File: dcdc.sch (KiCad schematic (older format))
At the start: 0 parts

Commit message: Added charge pump IC REG71050
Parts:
- added C1, C2: 2.2uF, symbol Device:C_Small
- added C3: 220nF, symbol Device:C_Small
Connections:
- new net +3V3: C1.1
- new net +5V: C2.1
- new net GNDREF: C1.2, C2.2
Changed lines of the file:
@@
 $Descr A4 11693 8268
 encoding utf-8
-Sheet 4 8
+Sheet 4 11
 Title ""
 Date ""
@@
 Comment4 ""
 $EndDescr
+$Comp
+L Matthias:REG71050 #U05
+U 1 1 5BCCE2ED
+P 5800 3700
+F 0 "#U05" H 5500 3300 50  0000 C CNN
+F 1 "REG71050" H 5650 4000 50  0000 C CNN
+F 2 "" H 5600 3700 50  0001 C CNN
+F 3 "" H 5600 3700 50  0001 C CNN
+	1    5800 3700
+	1    0    0    -1
+$EndComp
+$Comp
+L power:+3V3 #PWR0109
+U 1 1 5BCCE361
+P 4600 3500
+F 0 "#PWR0109" H 4600 3350 50  0001 C CNN
+F 1 "+3V3" H 4615 3673 50  0000 C CNN
+F 2 "" H 4600 3500 50  0001 C CNN
+F 3 "" H 4600 3500 50  0001 C CNN
+	1    4600 3500
+	1    0    0    -1
+$EndComp
+$Comp
+L power:+5V #PWR0110
+U 1 1 5BCCE38F
+P 7250 3450
+F 0 "#PWR0110" H 7250 3300 50  0001 C CNN
+F 1 "+5V" H 7265 3623 50  0000 C CNN
+F 2 "" H 7250 3450 50  0001 C CNN
+F 3 "" H 7250 3450 50  0001 C CNN
+	1    7250 3450
+	1    0    0    -1
+$EndComp
+$Comp
+L Device:C_Small C3
+U 1 1 5BCCE42B
+P 6600 3900
+F 0 "C3" H 6692 3946 50  0000 L CNN
+F 1 "220nF" H 6692 3855 50  0000 L CNN
+F 2 "" H 6600 3900 50  0001 C CNN
+F 3 "~" H 6600 3900 50  0001 C CNN
+	1    6600 3900
+	1    0    0    -1
+$EndComp
+Wire Wire Line
+	5350 3700 5250 3700
+Wire Wire Line
+	4600 3700 4600 3500
+Wire Wire Line
+	5350 3550 5250 3550
+Wire Wire Line
+	5250 3550 5250 3700
+Connection ~ 5250 3700
+Wire Wire Line
+	5250 3700 4600 3700
+Wire Wire Line
+	5350 3950 5250 3950
+Wire Wire Line
+	5250 3950 5250 4100
+$Comp
+L power:GNDREF #PWR0111
+U 1 1 5BCCE4F1
+P 5250 4100
+F 0 "#PWR0111" H 5250 3850 50  0001 C CNN
+F 1 "GNDREF" H 5255 3927 50  0000 C CNN
+F 2 "" H 5250 4100 50  0001 C CNN
+F 3 "" H 5250 4100 50  0001 C CNN
+	1    5250 4100
+	1    0    0    -1
+$EndComp
+Wire Wire Line
+	6250 3850 6400 3850
+Wire Wire Line
+	6400 3850 6400 3800
+Wire Wire Line
+	6400 3800 6600 3800
+Wire Wire Line
+	6250 3950 6400 3950
+Wire Wire Line
+	6400 3950 6400 4000
+Wire Wire Line
+	6400 4000 6600 4000
+$Comp
+L Device:C_Small C1
+U 1 1 5BCCE887
+P 4600 3800
+F 0 "C1" H 4692 3846 50  0000 L CNN
+F 1 "2.2uF" H 4692 3755 50  0000 L CNN
+F 2 "" H 4600 3800 50  0001 C CNN
+F 3 "~" H 4600 3800 50  0001 C CNN
+	1    4600 3800
+	1    0    0    -1
+$EndComp
+Connection ~ 4600 3700
+$Comp
+L Device:C_Small C2
+U 1 1 5BCCE8E1
+P 7250 3800
+F 0 "C2" H 7342 3846 50  0000 L CNN
+F 1 "2.2uF" H 7342 3755 50  0000 L CNN
+F 2 "" H 7250 3800 50  0001 C CNN
+F 3 "~" H 7250 3800 50  0001 C CNN
+	1    7250 3800
+	1    0    0    -1
+$EndComp
+Wire Wire Line
+	6250 3700 7250 3700
+Wire Wire Line
+	7250 3700 7250 3450
+Connection ~ 7250 3700
+$Comp
+L power:GNDREF #PWR0112
+U 1 1 5BCCEAA5
+P 4600 3900
+F 0 "#PWR0112" H 4600 3650 50  0001 C CNN
+F 1 "GNDREF" H 4605 3727 50  0000 C CNN
+F 2 "" H 4600 3900 50  0001 C CNN
+F 3 "" H 4600 3900 50  0001 C CNN
+	1    4600 3900
+	1    0    0    -1
+$EndComp
+$Comp
+L power:GNDREF #PWR0113
+U 1 1 5BCCEAB8
+P 7250 3900
+F 0 "#PWR0113" H 7250 3650 50  0001 C CNN
+F 1 "GNDREF" H 7255 3727 50  0000 C CNN
+F 2 "" H 7250 3900 50  0001 C CNN
+F 3 "" H 7250 3900 50  0001 C CNN
+	1    7250 3900
+	1    0    0    -1
+$EndComp
 $EndSCHEMATC

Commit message: Assigned footprints
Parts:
- C1, C2, C3: footprint (none) -> Capacitor_SMD:C_0805_2012Metric_Pad1.15x1.40mm_HandSolder
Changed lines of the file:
@@
 F 0 "#U05" H 5500 3300 50  0000 C CNN
 F 1 "REG71050" H 5650 4000 50  0000 C CNN
-F 2 "" H 5600 3700 50  0001 C CNN
+F 2 "Package_TO_SOT_SMD:SOT-23-6_Handsoldering" H 5600 3700 50  0001 C CNN
 F 3 "" H 5600 3700 50  0001 C CNN
 	1    5800 3700
@@
 F 0 "C3" H 6692 3946 50  0000 L CNN
 F 1 "220nF" H 6692 3855 50  0000 L CNN
-F 2 "" H 6600 3900 50  0001 C CNN
+F 2 "Capacitor_SMD:C_0805_2012Metric_Pad1.15x1.40mm_HandSolder" H 6600 3900 50  0001 C CNN
 F 3 "~" H 6600 3900 50  0001 C CNN
 	1    6600 3900
@@
 F 0 "C1" H 4692 3846 50  0000 L CNN
 F 1 "2.2uF" H 4692 3755 50  0000 L CNN
-F 2 "" H 4600 3800 50  0001 C CNN
+F 2 "Capacitor_SMD:C_0805_2012Metric_Pad1.15x1.40mm_HandSolder" H 4600 3800 50  0001 C CNN
 F 3 "~" H 4600 3800 50  0001 C CNN
 	1    4600 3800
@@
 F 0 "C2" H 7342 3846 50  0000 L CNN
 F 1 "2.2uF" H 7342 3755 50  0000 L CNN
-F 2 "" H 7250 3800 50  0001 C CNN
+F 2 "Capacitor_SMD:C_0805_2012Metric_Pad1.15x1.40mm_HandSolder" H 7250 3800 50  0001 C CNN
 F 3 "~" H 7250 3800 50  0001 C CNN
 	1    7250 3800

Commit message: Began layouting
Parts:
- added U5: REG71050, Package_TO_SOT_SMD:SOT-23-6_Handsoldering, symbol Matthias:REG71050
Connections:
- net +3V3: now also U5.3 (EN), U5.5 (V_IN)
- net +5V: now also U5.1 (V_OUT)
- net GNDREF: now also U5.2 (GND)
- net at C3.1: now also U5.4 (C_PUMP_A)
- net at C3.2: now also U5.6 (C_PUMP_B)
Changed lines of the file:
@@
 $EndDescr
 $Comp
-L Matthias:REG71050 #U05
+L Matthias:REG71050 U5
 U 1 1 5BCCE2ED
 P 5800 3700
-F 0 "#U05" H 5500 3300 50  0000 C CNN
+F 0 "U5" H 5500 3300 50  0000 C CNN
 F 1 "REG71050" H 5650 4000 50  0000 C CNN
 F 2 "Package_TO_SOT_SMD:SOT-23-6_Handsoldering" H 5600 3700 50  0001 C CNN

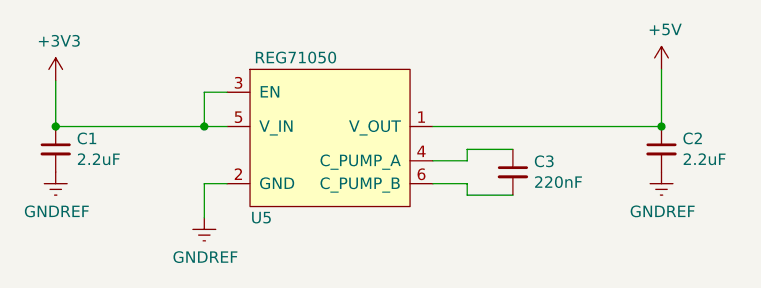
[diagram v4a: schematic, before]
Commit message: Continued layouting
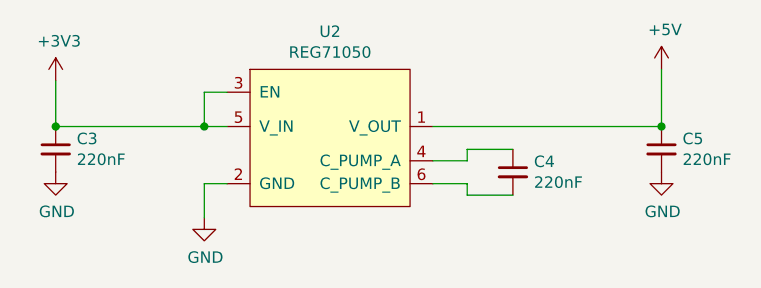
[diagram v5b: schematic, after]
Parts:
- removed C1, C2: 2.2uF, Capacitor_SMD:C_0805_2012Metric_Pad1.15x1.40mm_HandSolder, symbol Device:C_Small
- removed U5: REG71050, Package_TO_SOT_SMD:SOT-23-6_Handsoldering, symbol Matthias:REG71050
- added C3, C5: 220nF, Capacitor_SMD:C_0805_2012Metric_Pad1.15x1.40mm_HandSolder, symbol Device:C_Small
- added U2: REG71050, Package_TO_SOT_SMD:SOT-23-6_Handsoldering, symbol Matthias:REG71050
- renumbered C3 to C4
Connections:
- net +3V3: now also C3.1, U2.3 (EN), U2.5 (V_IN)
- net +5V: now also C5.1, U2.1 (V_OUT)
- net at C4.1: now also U2.4 (C_PUMP_A)
- net at C4.2: now also U2.6 (C_PUMP_B)
- new net GND: C3.2, C5.2, U2.2 (GND)
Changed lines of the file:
@@
 $EndDescr
 $Comp
-L Matthias:REG71050 U5
-U 1 1 5BCCE2ED
-P 5800 3700
-F 0 "U5" H 5500 3300 50  0000 C CNN
-F 1 "REG71050" H 5650 4000 50  0000 C CNN
-F 2 "Package_TO_SOT_SMD:SOT-23-6_Handsoldering" H 5600 3700 50  0001 C CNN
-F 3 "" H 5600 3700 50  0001 C CNN
-	1    5800 3700
-	1    0    0    -1
-$EndComp
-$Comp
-L power:+3V3 #PWR0109
+L power:+3V3 #PWR013
 U 1 1 5BCCE361
 P 4600 3500
-F 0 "#PWR0109" H 4600 3350 50  0001 C CNN
+F 0 "#PWR013" H 4600 3350 50  0001 C CNN
 F 1 "+3V3" H 4615 3673 50  0000 C CNN
 F 2 "" H 4600 3500 50  0001 C CNN
@@
 $EndComp
 $Comp
-L power:+5V #PWR0110
+L power:+5V #PWR016
 U 1 1 5BCCE38F
 P 7250 3450
-F 0 "#PWR0110" H 7250 3300 50  0001 C CNN
+F 0 "#PWR016" H 7250 3300 50  0001 C CNN
 F 1 "+5V" H 7265 3623 50  0000 C CNN
 F 2 "" H 7250 3450 50  0001 C CNN
@@
 $EndComp
 $Comp
-L Device:C_Small C3
+L Device:C_Small C4
 U 1 1 5BCCE42B
 P 6600 3900
-F 0 "C3" H 6692 3946 50  0000 L CNN
+F 0 "C4" H 6692 3946 50  0000 L CNN
 F 1 "220nF" H 6692 3855 50  0000 L CNN
 F 2 "Capacitor_SMD:C_0805_2012Metric_Pad1.15x1.40mm_HandSolder" H 6600 3900 50  0001 C CNN
@@
 Wire Wire Line
 	5250 3950 5250 4100
-$Comp
-L power:GNDREF #PWR0111
-U 1 1 5BCCE4F1
-P 5250 4100
-F 0 "#PWR0111" H 5250 3850 50  0001 C CNN
-F 1 "GNDREF" H 5255 3927 50  0000 C CNN
-F 2 "" H 5250 4100 50  0001 C CNN
-F 3 "" H 5250 4100 50  0001 C CNN
-	1    5250 4100
-	1    0    0    -1
-$EndComp
 Wire Wire Line
 	6250 3850 6400 3850
@@
 Wire Wire Line
 	6400 4000 6600 4000
+Wire Wire Line
+	6250 3700 7250 3700
+Wire Wire Line
+	7250 3700 7250 3450
 $Comp
-L Device:C_Small C1
-U 1 1 5BCCE887
+L Matthias:REG71050 U2
+U 1 1 5BCF6E97
+P 5800 3700
+F 0 "U2" H 5800 4115 50  0000 C CNN
+F 1 "REG71050" H 5800 4024 50  0000 C CNN
+F 2 "Package_TO_SOT_SMD:SOT-23-6_Handsoldering" H 5600 3700 50  0001 C CNN
+F 3 "" H 5600 3700 50  0001 C CNN
+	1    5800 3700
+	1    0    0    -1
+$EndComp
+$Comp
+L power:GND #PWR017
+U 1 1 5BCF70B8
+P 7250 3900
+F 0 "#PWR017" H 7250 3650 50  0001 C CNN
+F 1 "GND" H 7255 3727 50  0000 C CNN
+F 2 "" H 7250 3900 50  0001 C CNN
+F 3 "" H 7250 3900 50  0001 C CNN
+	1    7250 3900
+	1    0    0    -1
+$EndComp
+$Comp
+L power:GND #PWR015
+U 1 1 5BCF70D2
+P 5250 4100
+F 0 "#PWR015" H 5250 3850 50  0001 C CNN
+F 1 "GND" H 5255 3927 50  0000 C CNN
+F 2 "" H 5250 4100 50  0001 C CNN
+F 3 "" H 5250 4100 50  0001 C CNN
+	1    5250 4100
+	1    0    0    -1
+$EndComp
+$Comp
+L power:GND #PWR014
+U 1 1 5BCF70E5
+P 4600 3900
+F 0 "#PWR014" H 4600 3650 50  0001 C CNN
+F 1 "GND" H 4605 3727 50  0000 C CNN
+F 2 "" H 4600 3900 50  0001 C CNN
+F 3 "" H 4600 3900 50  0001 C CNN
+	1    4600 3900
+	1    0    0    -1
+$EndComp
+$Comp
+L Device:C_Small C5
+U 1 1 5BCF742B
+P 7250 3800
+F 0 "C5" H 7342 3846 50  0000 L CNN
+F 1 "220nF" H 7342 3755 50  0000 L CNN
+F 2 "Capacitor_SMD:C_0805_2012Metric_Pad1.15x1.40mm_HandSolder" H 7250 3800 50  0001 C CNN
+F 3 "~" H 7250 3800 50  0001 C CNN
+	1    7250 3800
+	1    0    0    -1
+$EndComp
+Connection ~ 7250 3700
+$Comp
+L Device:C_Small C3
+U 1 1 5BCF7461
 P 4600 3800
-F 0 "C1" H 4692 3846 50  0000 L CNN
-F 1 "2.2uF" H 4692 3755 50  0000 L CNN
+F 0 "C3" H 4692 3846 50  0000 L CNN
+F 1 "220nF" H 4692 3755 50  0000 L CNN
 F 2 "Capacitor_SMD:C_0805_2012Metric_Pad1.15x1.40mm_HandSolder" H 4600 3800 50  0001 C CNN
 F 3 "~" H 4600 3800 50  0001 C CNN
@@
 $EndComp
 Connection ~ 4600 3700
-$Comp
-L Device:C_Small C2
-U 1 1 5BCCE8E1
-P 7250 3800
-F 0 "C2" H 7342 3846 50  0000 L CNN
-F 1 "2.2uF" H 7342 3755 50  0000 L CNN
-F 2 "Capacitor_SMD:C_0805_2012Metric_Pad1.15x1.40mm_HandSolder" H 7250 3800 50  0001 C CNN
-F 3 "~" H 7250 3800 50  0001 C CNN
-	1    7250 3800
-	1    0    0    -1
-$EndComp
-Wire Wire Line
-	6250 3700 7250 3700
-Wire Wire Line
-	7250 3700 7250 3450
-Connection ~ 7250 3700
-$Comp
-L power:GNDREF #PWR0112
-U 1 1 5BCCEAA5
-P 4600 3900
-F 0 "#PWR0112" H 4600 3650 50  0001 C CNN
-F 1 "GNDREF" H 4605 3727 50  0000 C CNN
-F 2 "" H 4600 3900 50  0001 C CNN
-F 3 "" H 4600 3900 50  0001 C CNN
-	1    4600 3900
-	1    0    0    -1
-$EndComp
-$Comp
-L power:GNDREF #PWR0113
-U 1 1 5BCCEAB8
-P 7250 3900
-F 0 "#PWR0113" H 7250 3650 50  0001 C CNN
-F 1 "GNDREF" H 7255 3727 50  0000 C CNN
-F 2 "" H 7250 3900 50  0001 C CNN
-F 3 "" H 7250 3900 50  0001 C CNN
-	1    7250 3900
-	1    0    0    -1
-$EndComp
 $EndSCHEMATC

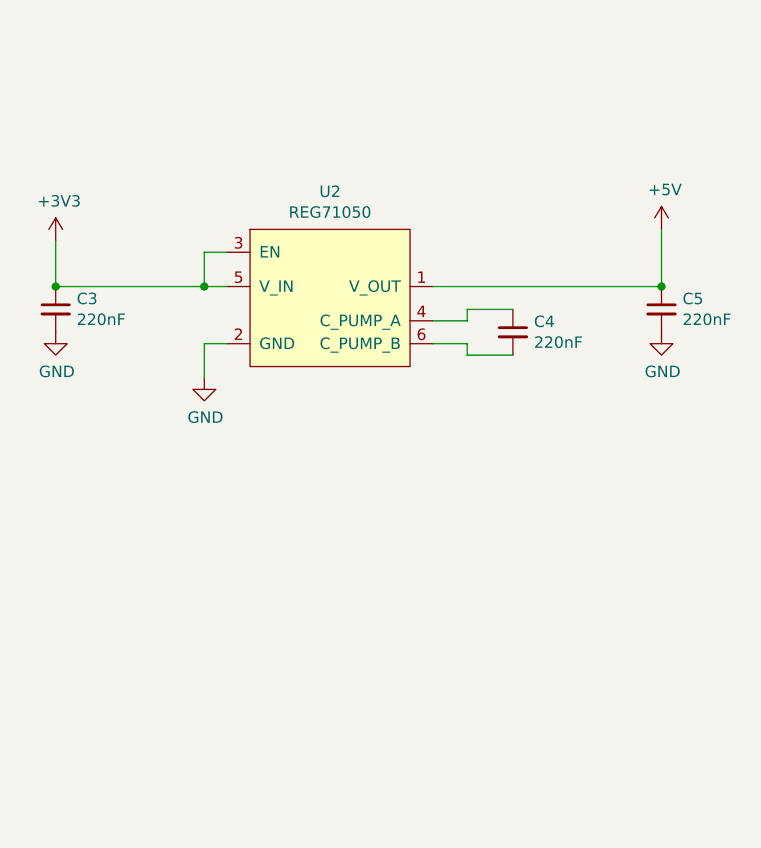
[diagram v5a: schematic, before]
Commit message: Updated RJ45 symbol and corresponding signal names
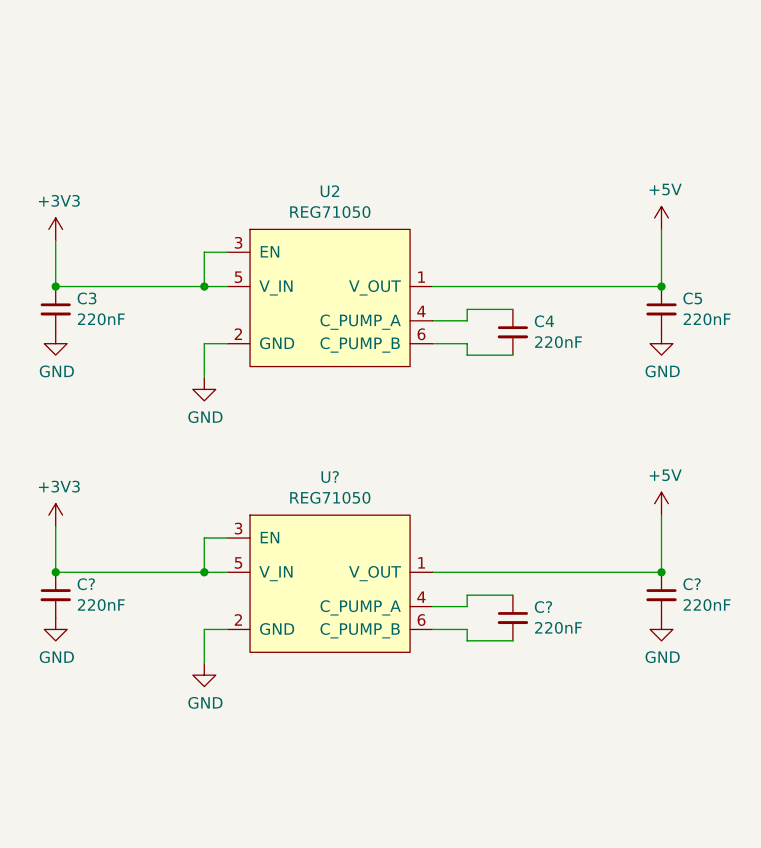
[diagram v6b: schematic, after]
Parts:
- added C? (x3): 220nF, Capacitor_SMD:C_0805_2012Metric_Pad1.15x1.40mm_HandSolder, symbol Device:C_Small
- added U?: REG71050, Package_TO_SOT_SMD:SOT-23-6_Handsoldering, symbol Matthias:REG71050
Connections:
- net +3V3: now also C?.1, U?.3 (EN), U?.5 (V_IN)
- net +5V: now also C?.1, U?.1 (V_OUT)
- net GND: now also C?.2, C?.2, U?.2 (GND)
- new net: C?.1, U?.4 (C_PUMP_A)
- new net: C?.2, U?.6 (C_PUMP_B)
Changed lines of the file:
@@
 $EndComp
 Connection ~ 4600 3700
+$Comp
+L power:+3V3 #PWR?
+U 1 1 5BE16F18
+P 4600 4750
+F 0 "#PWR?" H 4600 4600 50  0001 C CNN
+F 1 "+3V3" H 4615 4923 50  0000 C CNN
+F 2 "" H 4600 4750 50  0001 C CNN
+F 3 "" H 4600 4750 50  0001 C CNN
+	1    4600 4750
+	1    0    0    -1
+$EndComp
+$Comp
+L power:+5V #PWR?
+U 1 1 5BE16F1E
+P 7250 4700
+F 0 "#PWR?" H 7250 4550 50  0001 C CNN
+F 1 "+5V" H 7265 4873 50  0000 C CNN
+F 2 "" H 7250 4700 50  0001 C CNN
+F 3 "" H 7250 4700 50  0001 C CNN
+	1    7250 4700
+	1    0    0    -1
+$EndComp
+$Comp
+L Device:C_Small C?
+U 1 1 5BE16F24
+P 6600 5150
+F 0 "C?" H 6692 5196 50  0000 L CNN
+F 1 "220nF" H 6692 5105 50  0000 L CNN
+F 2 "Capacitor_SMD:C_0805_2012Metric_Pad1.15x1.40mm_HandSolder" H 6600 5150 50  0001 C CNN
+F 3 "~" H 6600 5150 50  0001 C CNN
+	1    6600 5150
+	1    0    0    -1
+$EndComp
+Wire Wire Line
+	5350 4950 5250 4950
+Wire Wire Line
+	4600 4950 4600 4750
+Wire Wire Line
+	5350 4800 5250 4800
+Wire Wire Line
+	5250 4800 5250 4950
+Connection ~ 5250 4950
+Wire Wire Line
+	5250 4950 4600 4950
+Wire Wire Line
+	5350 5200 5250 5200
+Wire Wire Line
+	5250 5200 5250 5350
+Wire Wire Line
+	6250 5100 6400 5100
+Wire Wire Line
+	6400 5100 6400 5050
+Wire Wire Line
+	6400 5050 6600 5050
+Wire Wire Line
+	6250 5200 6400 5200
+Wire Wire Line
+	6400 5200 6400 5250
+Wire Wire Line
+	6400 5250 6600 5250
+Wire Wire Line
+	6250 4950 7250 4950
+Wire Wire Line
+	7250 4950 7250 4700
+$Comp
+L Matthias:REG71050 U?
+U 1 1 5BE16F3B
+P 5800 4950
+F 0 "U?" H 5800 5365 50  0000 C CNN
+F 1 "REG71050" H 5800 5274 50  0000 C CNN
+F 2 "Package_TO_SOT_SMD:SOT-23-6_Handsoldering" H 5600 4950 50  0001 C CNN
+F 3 "" H 5600 4950 50  0001 C CNN
+	1    5800 4950
+	1    0    0    -1
+$EndComp
+$Comp
+L power:GND #PWR?
+U 1 1 5BE16F42
+P 7250 5150
+F 0 "#PWR?" H 7250 4900 50  0001 C CNN
+F 1 "GND" H 7255 4977 50  0000 C CNN
+F 2 "" H 7250 5150 50  0001 C CNN
+F 3 "" H 7250 5150 50  0001 C CNN
+	1    7250 5150
+	1    0    0    -1
+$EndComp
+$Comp
+L power:GND #PWR?
+U 1 1 5BE16F48
+P 5250 5350
+F 0 "#PWR?" H 5250 5100 50  0001 C CNN
+F 1 "GND" H 5255 5177 50  0000 C CNN
+F 2 "" H 5250 5350 50  0001 C CNN
+F 3 "" H 5250 5350 50  0001 C CNN
+	1    5250 5350
+	1    0    0    -1
+$EndComp
+$Comp
+L power:GND #PWR?
+U 1 1 5BE16F4E
+P 4600 5150
+F 0 "#PWR?" H 4600 4900 50  0001 C CNN
+F 1 "GND" H 4605 4977 50  0000 C CNN
+F 2 "" H 4600 5150 50  0001 C CNN
+F 3 "" H 4600 5150 50  0001 C CNN
+	1    4600 5150
+	1    0    0    -1
+$EndComp
+$Comp
+L Device:C_Small C?
+U 1 1 5BE16F54
+P 7250 5050
+F 0 "C?" H 7342 5096 50  0000 L CNN
+F 1 "220nF" H 7342 5005 50  0000 L CNN
+F 2 "Capacitor_SMD:C_0805_2012Metric_Pad1.15x1.40mm_HandSolder" H 7250 5050 50  0001 C CNN
+F 3 "~" H 7250 5050 50  0001 C CNN
+	1    7250 5050
+	1    0    0    -1
+$EndComp
+Connection ~ 7250 4950
+$Comp
+L Device:C_Small C?
+U 1 1 5BE16F5C
+P 4600 5050
+F 0 "C?" H 4692 5096 50  0000 L CNN
+F 1 "220nF" H 4692 5005 50  0000 L CNN
+F 2 "Capacitor_SMD:C_0805_2012Metric_Pad1.15x1.40mm_HandSolder" H 4600 5050 50  0001 C CNN
+F 3 "~" H 4600 5050 50  0001 C CNN
+	1    4600 5050
+	1    0    0    -1
+$EndComp
+Connection ~ 4600 4950
 $EndSCHEMATC

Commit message: Began redesigning with Si8660
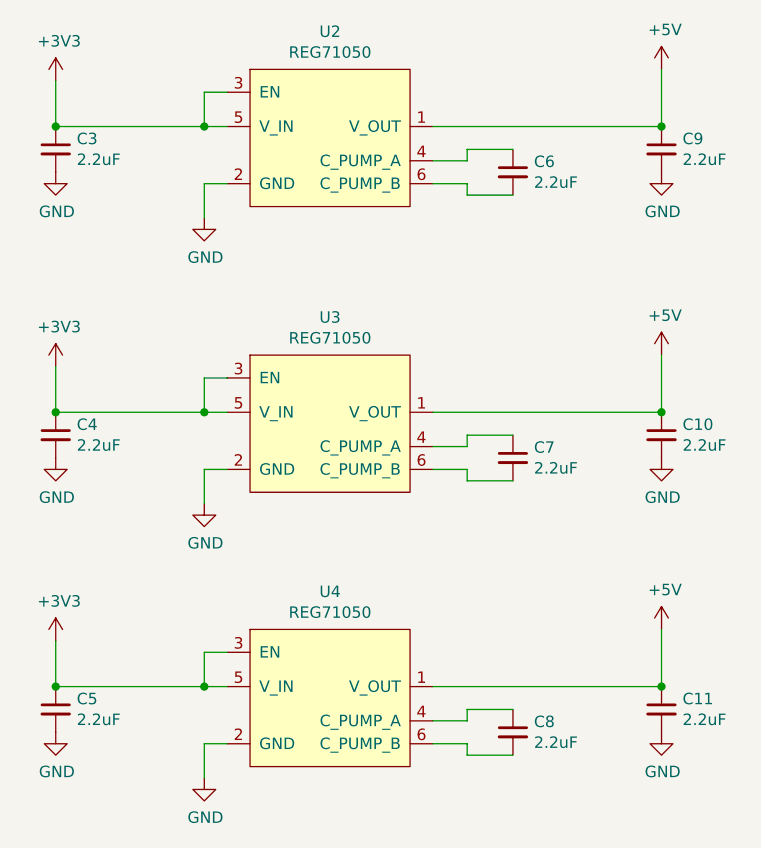
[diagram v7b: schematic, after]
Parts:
- added C11, C5, C8: 2.2uF, Capacitor_SMD:C_0805_2012Metric_Pad1.15x1.40mm_HandSolder, symbol Device:C_Small
- added U4: REG71050, Package_TO_SOT_SMD:SOT-23-6_Handsoldering, symbol Matthias:REG71050
- C10, C4, C7: renamed from C?; value 220nF -> 2.2uF
- C3: value 220nF -> 2.2uF
- C6: renamed from C4; value 220nF -> 2.2uF
- C9: renamed from C5; value 220nF -> 2.2uF
- gave numbers to parts that had none: 1
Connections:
- net +3V3: now also C5.1, U4.3 (EN), U4.5 (V_IN)
- net +5V: now also C11.1, U4.1 (V_OUT)
- net GND: now also C11.2, C5.2, U4.2 (GND)
- new net: C8.1, U4.4 (C_PUMP_A)
- new net: C8.2, U4.6 (C_PUMP_B)
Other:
- moved on the sheet: C10, C3, C4, C6, C7, C9, U2, U3
